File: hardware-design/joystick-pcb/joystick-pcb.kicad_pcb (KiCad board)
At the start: 2 copper layers, 20 x 20 mm, 6 parts, among them J1 Wire_Pads, SW1 SKRHABE010

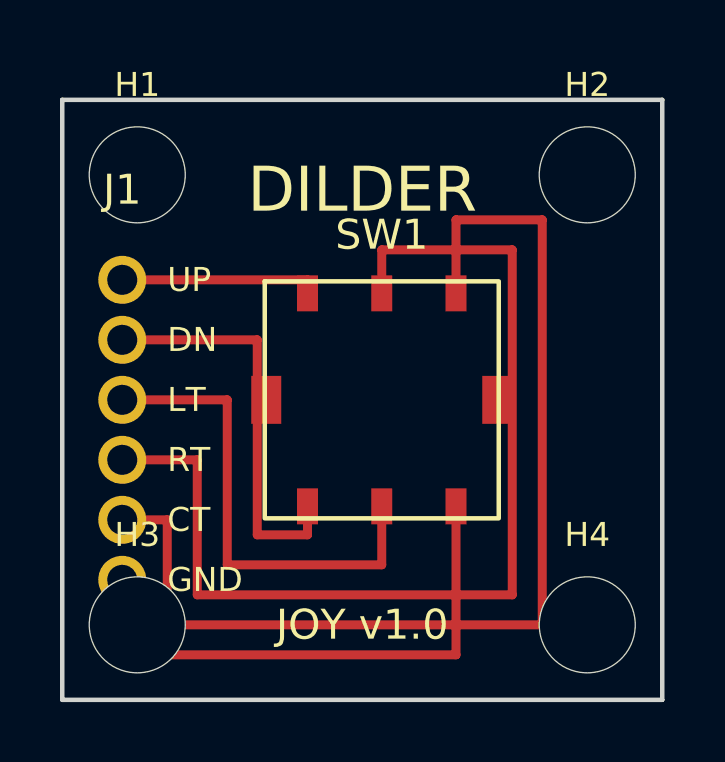
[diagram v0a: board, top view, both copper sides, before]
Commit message: Joystick PCB Rev 2.0 — kleeb footprint, datasheet pinout, headless autoroute
Rev 1 of the joystick breakout shipped with three real bugs: a hand-drawn
SKRHABE010 footprint with the wrong pad geometry, a wire pad that
physically overlapped a mounting hole, and three pin assignments that
didn't match the Alps datasheet. Rev 2.0 fixes all three by cloning
proven references and adding machine-checkable verification.

PCB / schematic
- Footprint: cloned from crides/kleeb SKRHA-boss (production-tested in
  shipping keyboards), rotated -45° so pads land axis-aligned on the
  body's left/right faces. Includes the two NPTH alignment posts and
  two SMD anchor pads from the source.
- Pin names confirmed against the Alps SKRHABE010 datasheet circuit
  diagram (1=A, 2=Center, 3=C, 4=B, 5=Common, 6=D). Rev 1 had pins 2,
  5, and 6 wrong.
- Wire pads repositioned to bottom edge at 1.8mm pitch, 1.4mm OD /
  0.8mm drill. All clearances verified by Python script before drawing
  (0.74mm min pad↔hole, 1.0mm pad↔pad, 2.30mm to board edge).
- Schematic rebuilt from scratch using the kleeb symbol with proper
  pin names (A/Center/C/B/Common/D) and label-stub style routing.

Routing
- Autorouted headlessly via the official Freerouting Docker image
  (ghcr.io/freerouting/freerouting), with DSN export/SES import done
  through the pcbnew Python module. No GUI interaction required.
- 23 trace segments + 1 through-hole via, 534mm total length.
- 8 bends, all 45°. Zero 90° corners. 0 clearance violations.
- KiCad CLI DRC: 0 copper violations, 0 unconnected nets, 0 schematic
  parity issues.

Documentation
- New hardware-design/HARDWARE-DESIGN-PROCESS.md — retrospective on the
  SCAD→print and PCB→fab loops with concrete improvements to cut
  wasted prints (calibration coupons, SVG cross-sections, presets-
  instead-of-prints, mandatory dimension comment blocks).
- New hardware-design/scad Parts/README.md — documents the three
  Python helpers (scad-export.py, bake-preset.py, export-preset.py)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
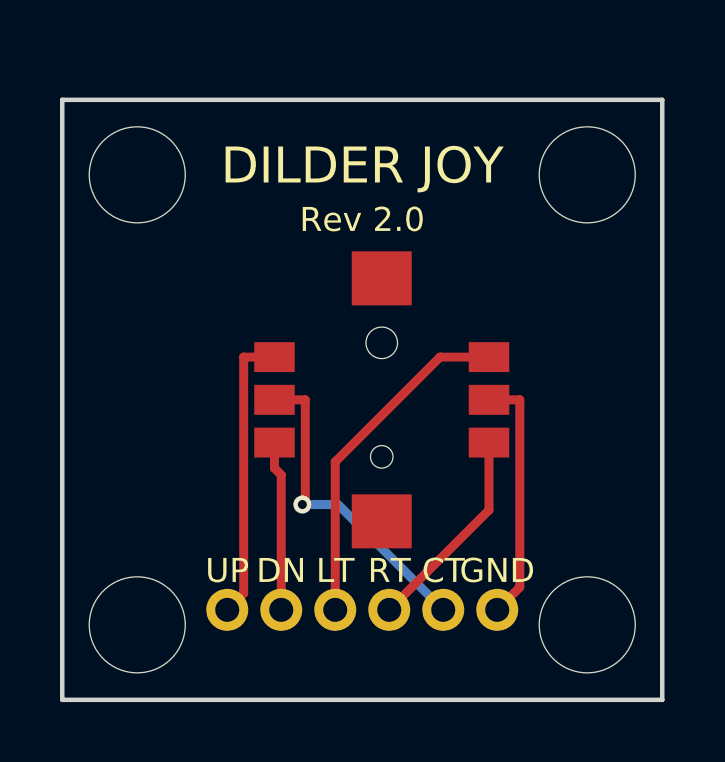
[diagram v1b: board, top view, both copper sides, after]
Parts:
- J1: footprint joystick-pcb:WirePads_1x06_P2.0mm -> joystick-pcb:WirePads_1x06_P1.8mm
- moved J1 10.0 mm to (110.0, 117.0)
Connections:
- SW1 pad 2: JOY_DOWN -> JOY_CENTER
- SW1 pad 3: JOY_LEFT -> JOY_DOWN
- SW1 pad 4: JOY_RIGHT -> JOY_LEFT
- SW1 pad 5: JOY_CENTER -> GND
- SW1 pad 6: GND -> JOY_RIGHT
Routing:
- net JOY_RIGHT: track 34.8 -> 6.95 mm
- net JOY_CENTER: track 36.3 -> 11.3 mm, vias 0 -> 1
- net GND: track 18.6 -> 8.34 mm
- net JOY_DOWN: track 13.6 -> 5.67 mm
- net JOY_LEFT: track 16.1 -> 11.5 mm
- net JOY_UP: track 6.62 -> 9.68 mm
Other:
- board text added: "DILDER JOY"
- board text added: "Rev 2.0"
- board text removed: "DILDER"
- board text removed: "JOY v1.0"
